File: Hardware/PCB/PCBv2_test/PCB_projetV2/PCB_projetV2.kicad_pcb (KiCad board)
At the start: 4 copper layers, 63.1 x 41.1 mm, 43 parts, among them J1 Conn_01x02, J10 Conn_02x03_Odd_Even, J11 R-78B5.0-2.0, J12 Conn_01x04, J13 Conn_01x02, J14 Conn_01x02, J2 Conn_01x04, J3 BU33SD5WG-TR, J4 Conn_01x06, J5 Conn_01x03, J6 Conn_01x03, J7 Conn_ST_STDC14, J8 Conn_01x06, J9 Conn_01x06, U1 STM32L552CCTx

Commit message: finalisation PCB v2
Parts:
- added G***: LOGO, LogoEnsea:LogoEnsea, F.Cu at (125.7, 86.7)
- added G***: LOGO, LogoAres:logoares, F.Cu at (125.5, 101.0)
- C1, C2, J2, J3: moved to F.Cu
- J5, J6: footprint Connector_JST:JST_XH_B3B-XH-A_1x03_P2.50mm_Vertical -> Connector_JST:JST_PH_B3B-PH-K_1x03_P2.00mm_Vertical
- moved J13 48.3 mm to (125.3, 93.7)
- moved J2 38.3 mm to (168.9, 78.0), turned to -90 degrees
- moved J14 26.5 mm to (142.6, 99.3), turned to 180 degrees
- moved C2 12.4 mm to (167.7, 93.9), turned to 0 degrees
- moved J3 9.34 mm to (167.7, 96.9), turned to 90 degrees
- moved TP2 6.63 mm to (167.3, 96.1), turned to 0 degrees
- moved L1 3.08 mm to (160.2, 100.8)
- moved C9 2.71 mm to (151.7, 96.0)
- moved C12 2.62 mm to (153.9, 87.2)
- moved C7 2.59 mm to (152.0, 97.8)
- moved U1 2.59 mm to (157.7, 92.3)
- moved C8 2.59 mm to (154.6, 98.6)
- moved C1 2.36 mm to (168.8, 100.8), turned to -90 degrees
- moved C13 2.24 mm to (158.9, 98.2)
- moved C14 2.20 mm to (158.9, 99.5)
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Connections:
- net +7.5V renamed +12V
- U1 pad 32: AIN1 -> AIN2
- U1 pad 33: AIN2 -> AIN1
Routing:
- net STLINK_RX: track 0.00 -> 39.4 mm, vias 0 -> 2
- net EncoderA2: track 0.00 -> 35.6 mm
- net EncoderA1: track 0.00 -> 35.6 mm
- net EncoderB2: track 0.00 -> 32.2 mm, vias 0 -> 1
- net EncoderB1: track 0.00 -> 30.7 mm, vias 0 -> 1
- net SWDIO: track 0.00 -> 28.6 mm, vias 0 -> 2
- net NRST: track 0.00 -> 28.4 mm, vias 0 -> 2
- net Rasp_TX: track 0.00 -> 26.9 mm, vias 0 -> 2
- net HC05_TX: track 0.00 -> 24.0 mm, vias 0 -> 2
- net SWCLK: track 0.00 -> 23.2 mm, vias 0 -> 2
- net STLINK_TX: track 0.00 -> 23.0 mm, vias 0 -> 2
- net Rasp_RX: track 0.00 -> 22.8 mm, vias 0 -> 2
- net HC05_RX: track 0.00 -> 22.6 mm, vias 0 -> 2
- net PWM_Servo1: track 0.00 -> 18.7 mm, vias 0 -> 2
- net PWMA: track 0.00 -> 18.4 mm, vias 0 -> 2
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- added copper zone on B.Cu, net +12V
- added copper zone on F.Cu, net +12V
- added copper zone on In2.Cu, net +12V
- added copper zone on F.Cu, net +3.3V
- added copper zone on In2.Cu, net +3.3V
- added copper zone on F.Cu, net +3.3VA
- added copper zone on B.Cu, net +5V
- added copper zone on F.Cu, net +5V
- added copper zone on In2.Cu, net +5V
- added copper zone on F.Cu, net AO1
- added copper zone on F.Cu, net AO2
- added copper zone on F.Cu, net BO1
- added copper zone on F.Cu, net BO2
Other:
- board size 63.1 x 41.1 mm -> 63.4 x 41.1 mm
- board text added: "CAPODAGLI Janus"
- board text added: "Projet 1A"

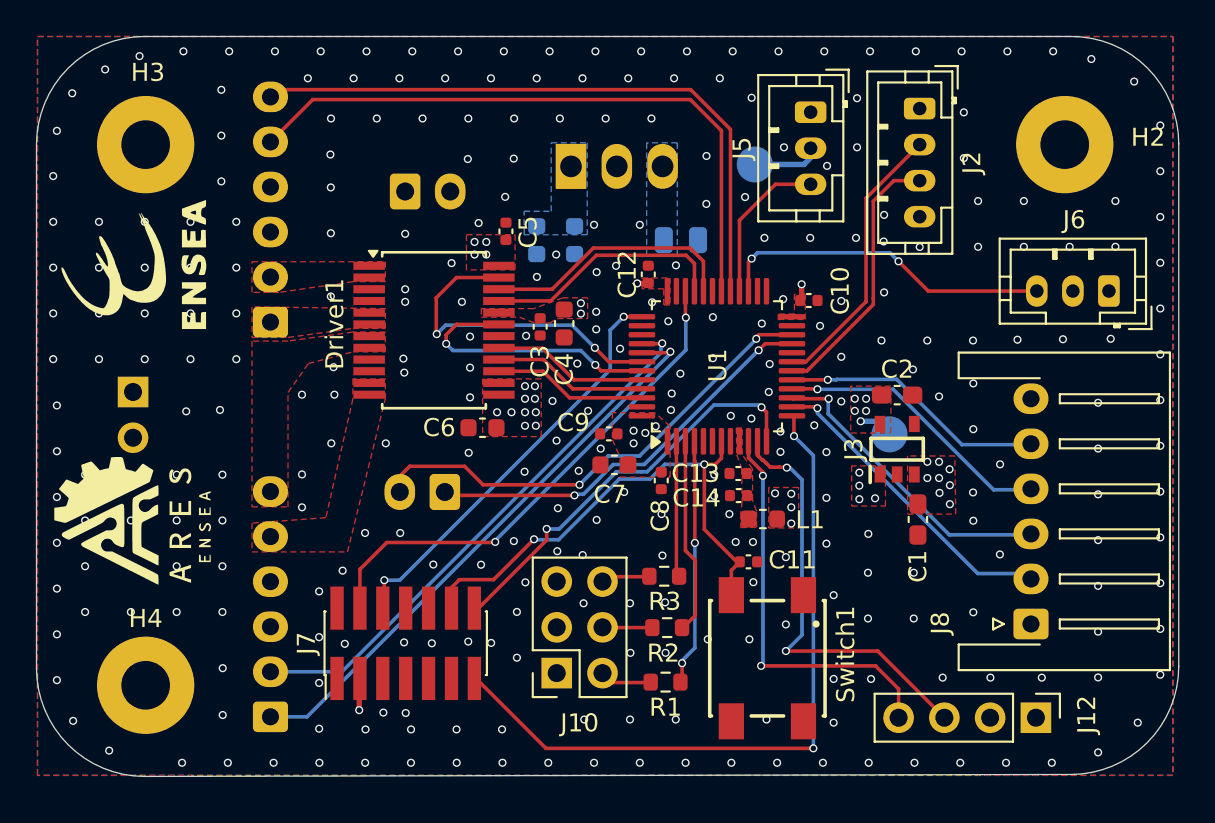
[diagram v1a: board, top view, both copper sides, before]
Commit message: ajout des condensateurs pour les modules
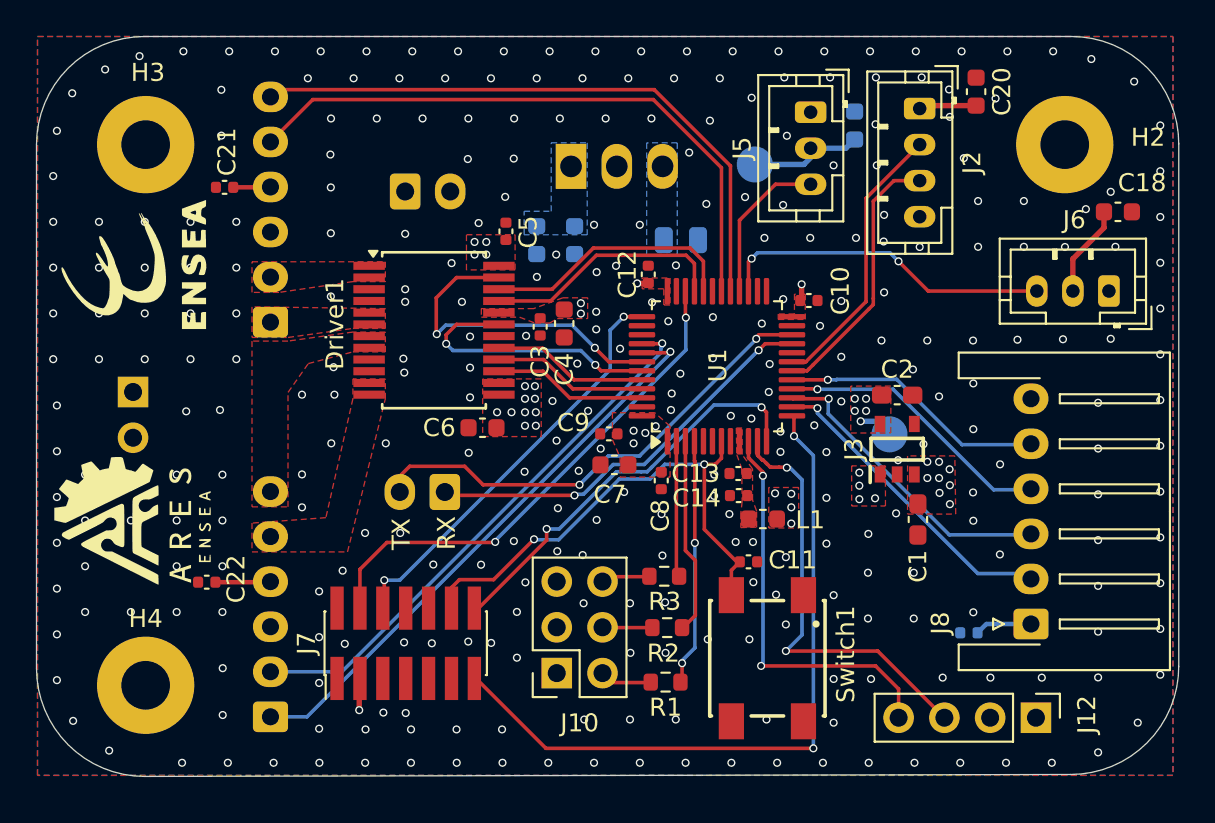
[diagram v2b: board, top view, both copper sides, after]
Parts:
- added C18: 10u, Capacitor_SMD:C_0603_1608Metric, F.Cu at (179.9, 83.7)
- added C19: 10u, Capacitor_SMD:C_0603_1608Metric, B.Cu at (165.3, 78.9)
- added C20: 10u, Capacitor_SMD:C_0603_1608Metric, F.Cu at (172.1, 77.1)
- added C21: 100n, Capacitor_SMD:C_0402_1005Metric, F.Cu at (130.4, 82.4)
- added C22: 100n, Capacitor_SMD:C_0402_1005Metric, F.Cu at (129.4, 104.3)
- added C23: 100n, Capacitor_SMD:C_0402_1005Metric, B.Cu at (171.7, 107.1)
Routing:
- net +5V: track 3.29 -> 17.4 mm
- net +3.3V: track 5.23 -> 10.4 mm
- net EncoderA2: track 35.6 -> 34.4 mm
- net EncoderA1: track 35.6 -> 34.4 mm
- net GND: vias 307 -> 319
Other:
- board text added: "GND"
- board text added: "RX"
- board text added: "TX"
- board text added: "VCC"

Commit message: amélioration finale PCB
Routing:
- net GND: vias 319 -> 321
- net +5V: vias 12 -> 20
- net +3.3V: vias 18 -> 26
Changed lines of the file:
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@@
 	)
 	(via
+		(at 165.69 90.58)
+		(size 0.45)
+		(drill 0.3)
+		(layers "F.Cu" "B.Cu")
+		(free yes)
+		(net 1)
+	)
+	(via
 		(at 125.95 86.825)
 		(size 0.45)
@@
 	)
 	(via
+		(at 157.11 81.57)
+		(size 0.45)
+		(drill 0.3)
+		(layers "F.Cu" "B.Cu")
+		(free yes)
+		(net 1)
+	)
+	(via
 		(at 148.575 94.225)
 		(size 0.45)
@@
 	)
 	(via
-		(at 153.42 84.45)
+		(at 153.27 84.49)
 		(size 0.45)
 		(drill 0.3)
@@
 	)
 	(via
+		(at 155.23 83.6)
+		(size 0.45)
+		(drill 0.3)
+		(layers "F.Cu" "B.Cu")
+		(free yes)
+		(net 2)
+	)
+	(via
 		(at 165.6 98.2)
 		(size 0.45)
@@
 	)
 	(via
+		(at 154.17 83.58)
+		(size 0.45)
+		(drill 0.3)
+		(layers "F.Cu" "B.Cu")
+		(free yes)
+		(net 2)
+	)
+	(via
+		(at 154.15 84.27)
+		(size 0.45)
+		(drill 0.3)
+		(layers "F.Cu" "B.Cu")
+		(free yes)
+		(net 2)
+	)
+	(via
 		(at 170.60793 98.014965)
 		(size 0.45)
@@
 	)
 	(via
+		(at 154.14 82.86)
+		(size 0.45)
+		(drill 0.3)
+		(layers "F.Cu" "B.Cu")
+		(free yes)
+		(net 2)
+	)
+	(via
 		(at 170.625 98.9)
 		(size 0.45)
@@
 	)
 	(via
+		(at 154.69 83.96)
+		(size 0.45)
+		(drill 0.3)
+		(layers "F.Cu" "B.Cu")
+		(free yes)
+		(net 2)
+	)
+	(via
+		(at 155.24 82.91)
+		(size 0.45)
+		(drill 0.3)
+		(layers "F.Cu" "B.Cu")
+		(free yes)
+		(net 2)
+	)
+	(via
 		(at 165.6 99.675)
 		(size 0.45)
@@
 	)
 	(via
+		(at 155.23 84.26)
+		(size 0.45)
+		(drill 0.3)
+		(layers "F.Cu" "B.Cu")
+		(free yes)
+		(net 2)
+	)
+	(via
 		(at 170.625 99.95)
 		(size 0.45)
@@
 		(net 2)
 	)
+	(via
+		(at 154.71 83.24)
+		(size 0.45)
+		(drill 0.3)
+		(layers "F.Cu" "B.Cu")
+		(free yes)
+		(net 2)
+	)
 	(segment
 		(start 175.125 106.6)
@@
 	)
 	(via
+		(at 166.09 92.52)
+		(size 0.45)
+		(drill 0.3)
+		(layers "F.Cu" "B.Cu")
+		(free yes)
+		(net 3)
+	)
+	(via
 		(at 137.85 111.38)
 		(size 0.45)
@@
 	)
 	(via
+		(at 166.72 91.83)
+		(size 0.45)
+		(drill 0.3)
+		(layers "F.Cu" "B.Cu")
+		(free yes)
+		(net 3)
+	)
+	(via
+		(at 166.08 91.83)
+		(size 0.45)
+		(drill 0.3)
+		(layers "F.Cu" "B.Cu")
+		(free yes)
+		(net 3)
+	)
+	(via
 		(at 165.675 95.35)
 		(size 0.45)
@@
 	)
 	(via
+		(at 167.41 91.83)
+		(size 0.45)
+		(drill 0.3)
+		(layers "F.Cu" "B.Cu")
+		(free yes)
+		(net 3)
+	)
+	(via
 		(at 165.975 94.775)
 		(size 0.45)
@@
 	)
 	(via
+		(at 165.44 92.525)
+		(size 0.45)
+		(drill 0.3)
+		(layers "F.Cu" "B.Cu")
+		(free yes)
+		(net 3)
+	)
+	(via
 		(at 153.275 87.7)
 		(size 0.45)
@@
 	)
 	(via
+		(at 167.42 92.5)
+		(size 0.45)
+		(drill 0.3)
+		(layers "F.Cu" "B.Cu")
+		(free yes)
+		(net 3)
+	)
+	(via
 		(at 150.15 88.8)
 		(size 0.45)
@@
 	)
 	(via
+		(at 165.43 91.81)
+		(size 0.45)
+		(drill 0.3)
+		(layers "F.Cu" "B.Cu")
+		(free yes)
+		(net 3)
+	)
+	(via
 		(at 160.925 99.35)
 		(size 0.45)
@@
 		(net 3)
 	)
+	(via
+		(at 166.73 92.51)
+		(size 0.45)
+		(drill 0.3)
+		(layers "F.Cu" "B.Cu")
+		(free yes)
+		(net 3)
+	)
 	(segment
 		(start 166.55 95.35)
@@
 	)
 	(segment
-		(start 164.35 93.025)
-		(end 167.675 93.025)
+		(start 163.85 93.05)
+		(end 167.7 93.05)
 		(width 0.2)
 		(layer "B.Cu")
@@
 	)
 	(segment
-		(start 175.075 96.65)
-		(end 175.125 96.6)
-		(width 0.2)
-		(layer "B.Cu")
-		(net 30)
-	)
-	(segment
-		(start 167.675 93.025)
+		(start 167.7 93.05)
 		(end 171.3 96.65)
 		(width 0.2)
@@
 	)
 	(segment
-		(start 164.325 93.05)
-		(end 164.35 93.025)
-		(width 0.2)
-		(layer "B.Cu")
-		(net 30)
-	)
-	(segment
-		(start 163.85 93.05)
-		(end 164.325 93.05)
+		(start 175.075 96.65)
+		(end 175.125 96.6)
 		(width 0.2)
 		(layer "B.Cu")
@@
 	)
 	(zone
+		(net 0)
+		(net_name "")
+		(layer "F.Cu")
+		(hatch edge 0.5)
+		(connect_pads
+			(clearance 0)
+		)
+		(min_thickness 0.25)
+		(filled_areas_thickness no)
+		(keepout
+			(tracks allowed)
+			(vias allowed)
+			(pads allowed)
+			(copperpour not_allowed)
+			(footprints allowed)
+		)
+		(placement
+			(enabled no)
+			(sheetname "")
+		)
+		(fill
+			(thermal_gap 0.5)
+			(thermal_bridge_width 0.5)
+		)
+		(polygon
+			(pts
+				(xy 167.86 96.05) (xy 168.17 96.05) (xy 168.17 95.99) (xy 167.86 95.99)
+			)
+		)
+	)
+	(zone
+		(net 2)
+		(net_name "+5V")
+		(layer "F.Cu")
+		(hatch edge 0.5)
+		(priority 22)
+		(connect_pads yes
+			(clearance 0.2)
+		)
+		(min_thickness 0.25)
+		(filled_areas_thickness no)
+		(fill yes
+			(thermal_gap 0.5)
+			(thermal_bridge_width 0.5)
+		)
+		(polygon
+			(pts
+				(xy 153.81 79.94) (xy 153.81 84.564553) (xy 155.548245 84.574542) (xy 155.57 79.93)
+			)
+		)
+	)
+	(zone
 		(net 3)
 		(net_name "+3.3V")
@@
 		(polygon
 			(pts
-				(xy 165.125 93.4) (xy 165.125 96) (xy 167.35 96) (xy 167.35 93.4)
+				(xy 165.125 91.52) (xy 165.125 96) (xy 167.67 96) (xy 167.67 91.52)
 			)
 		)
